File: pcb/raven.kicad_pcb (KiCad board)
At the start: 4 copper layers, 63.2 x 54.2 mm, 191 parts, among them J1 Conn_02x20_Odd_Even, J10 Conn_ARM_SWD_TagConnect_TC203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, J14 Conn_01x04_Pin, J15 Conn_01x04_Pin, J16 Conn_01x04_Pin, J17 Conn_01x04_Pin, J18 Conn_01x04_Pin, J2 Conn_01x04_MountingPin, J20 Screw_Terminal_01x02, J21 Conn_01x03_Pin, J22 Conn_01x03_Pin, J23 Conn_01x03_Pin, J24 Conn_01x03_Pin, J25 Conn_01x03_Pin, J26 Screw_Terminal_01x02, J27 Screw_Terminal_01x02, J28 Screw_Terminal_01x02, J29 Screw_Terminal_01x02, J3 Conn_01x02_Pin, J4 Conn_01x02_Pin, J5 Conn_01x04_MountingPin, J6 Conn_01x02_Pin, J7 Conn_01x02_Pin, J8 Conn_01x02_Pin, J9 Conn_01x02_Pin, SW1 SW_Push, SW2 SW_Push, U1 DRV8874PWPR, U2 ICM-42688-P, U3 QMC5883L, U30 DRV8874PWPR, U4 DRV8874PWPR, U5 DRV8874PWPR, U6 DRV8874PWPR, U7 STM32G431CBUx, U8 74HC595, U9 TPS548B28RWWR, Y1 16MHz

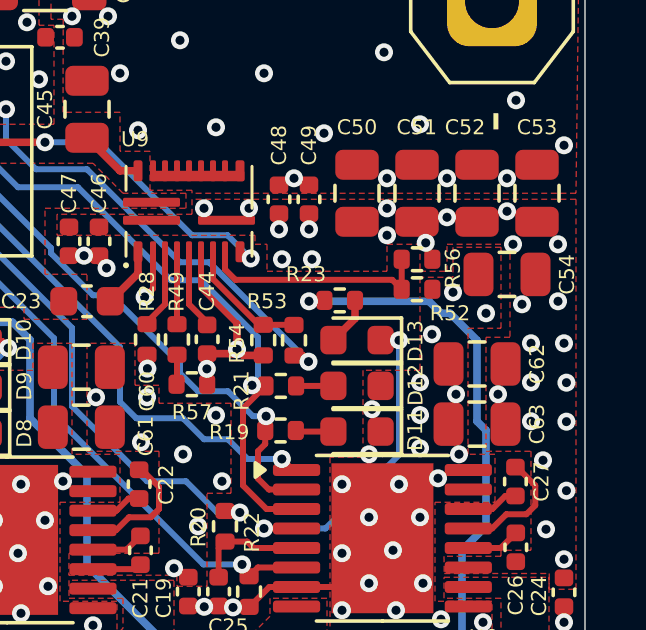
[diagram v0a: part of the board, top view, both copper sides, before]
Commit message: Change cutoff voltage
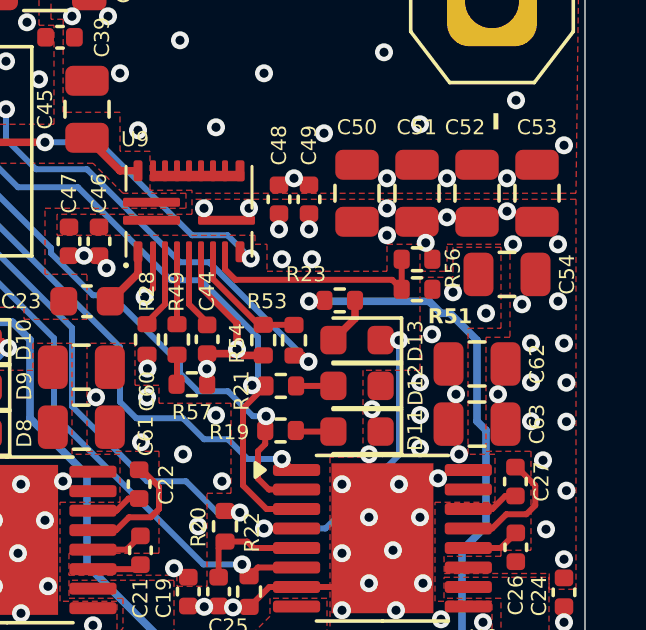
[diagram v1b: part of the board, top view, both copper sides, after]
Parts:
- removed R52: 12k, Resistor_SMD:R_0402_1005Metric
- added R51: 10k, Resistor_SMD:R_0402_1005Metric, F.Cu at (155.0, 80.0)

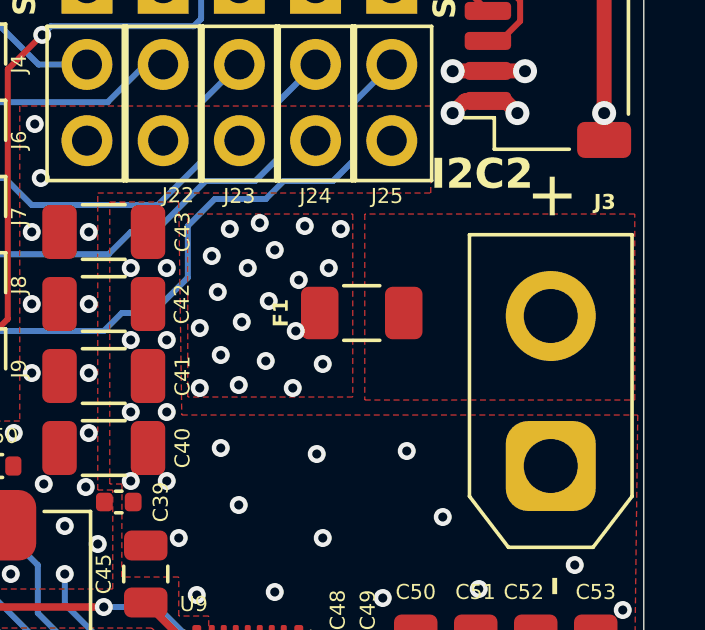
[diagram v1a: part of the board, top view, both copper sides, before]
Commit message: Plan adding power switch
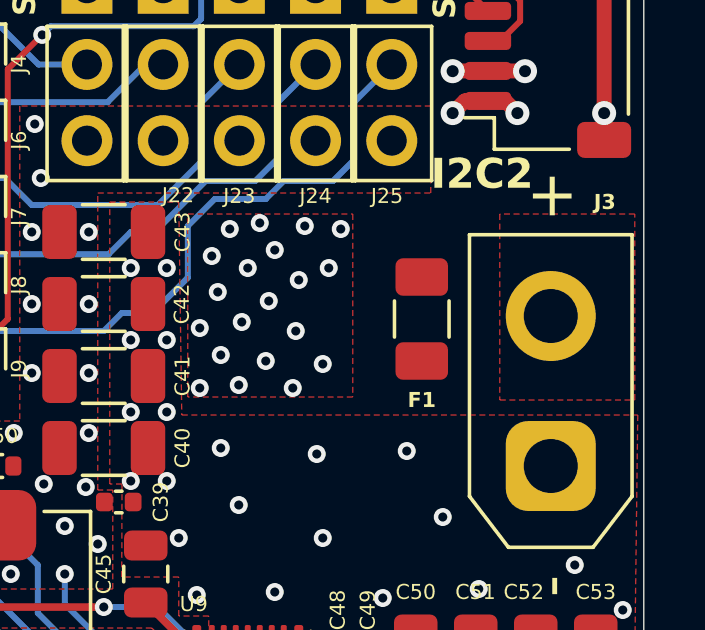
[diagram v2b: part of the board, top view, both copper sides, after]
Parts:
- moved F1 2.01 mm to (153.2, 65.5), turned to 90 degrees
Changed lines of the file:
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@@
 	(footprint "Fuse:Fuse_1206_3216Metric"
 		(layer "F.Cu")
-		(at 151.2 65.3)
+		(at 153.2 65.5 90)
 		(descr "Fuse SMD 1206 (3216 Metric), square (rectangular) end terminal, IPC_7351 nominal, (Body size source: http://www.tortai-tech.com/upload/download/2011102023233369053.pdf), generated with kicad-footprint-generator")
 		(tags "fuse")
 		(property "Reference" "F1"
-			(at -2.7 0 90)
+			(at -2.7 0 360)
 			(layer "F.SilkS")
 			(effects
@@
 		)
 		(property "Value" "Fuse"
-			(at 0 1.82 0)
+			(at 0 1.82 90)
 			(layer "F.Fab")
 			(effects
@@
 		)
 		(property "Footprint" "Fuse:Fuse_1206_3216Metric"
-			(at 0 0 0)
+			(at 0 0 90)
 			(unlocked yes)
 			(layer "F.Fab")
@@
 		)
 		(property "Datasheet" ""
-			(at 0 0 0)
+			(at 0 0 90)
 			(unlocked yes)
 			(layer "F.Fab")
@@
 		)
 		(property "Description" "Fuse"
-			(at 0 0 0)
+			(at 0 0 90)
 			(unlocked yes)
 			(layer "F.Fab")
@@
 		)
 		(property "LCSC" "C2838917"
-			(at 0 0 0)
+			(at 0 0 90)
 			(unlocked yes)
 			(layer "F.Fab")
@@
 		)
 		(fp_line
-			(start -2.28 -1.12)
-			(end 2.28 -1.12)
+			(start 2.28 -1.12)
+			(end 2.28 1.12)
 			(stroke
 				(width 0.05)
@@
 		)
 		(fp_line
-			(start -2.28 1.12)
-			(end -2.28 -1.12)
+			(start -2.28 -1.12)
+			(end 2.28 -1.12)
 			(stroke
 				(width 0.05)
@@
 		)
 		(fp_line
-			(start 2.28 -1.12)
-			(end 2.28 1.12)
+			(start 2.28 1.12)
+			(end -2.28 1.12)
 			(stroke
 				(width 0.05)
@@
 		)
 		(fp_line
-			(start 2.28 1.12)
-			(end -2.28 1.12)
+			(start -2.28 1.12)
+			(end -2.28 -1.12)
 			(stroke
 				(width 0.05)
@@
 		)
 		(fp_line
-			(start -1.6 -0.8)
-			(end 1.6 -0.8)
+			(start 1.6 -0.8)
+			(end 1.6 0.8)
 			(stroke
 				(width 0.1)
@@
 		)
 		(fp_line
-			(start -1.6 0.8)
-			(end -1.6 -0.8)
+			(start -1.6 -0.8)
+			(end 1.6 -0.8)
 			(stroke
 				(width 0.1)
@@
 		)
 		(fp_line
-			(start 1.6 -0.8)
-			(end 1.6 0.8)
+			(start 1.6 0.8)
+			(end -1.6 0.8)
 			(stroke
 				(width 0.1)
@@
 		)
 		(fp_line
-			(start 1.6 0.8)
-			(end -1.6 0.8)
+			(start -1.6 0.8)
+			(end -1.6 -0.8)
 			(stroke
 				(width 0.1)
@@
 		)
 		(fp_text user "${REFERENCE}"
-			(at 0 0 0)
+			(at 0 0 90)
 			(layer "F.Fab")
 			(effects
@@
 		)
 		(pad "1" smd roundrect
-			(at -1.399999 0)
+			(at -1.399999 0 90)
 			(size 1.25 1.75)
 			(layers "F.Cu" "F.Paste" "F.Mask")
@@
 		)
 		(pad "2" smd roundrect
-			(at 1.399999 0)
+			(at 1.399999 0 90)
 			(size 1.25 1.75)
 			(layers "F.Cu" "F.Paste" "F.Mask")
@@
 		(min_thickness 0.25)
 		(filled_areas_thickness no)
-		(fill yes
+		(fill
 			(thermal_gap 0.5)
 			(thermal_bridge_width 0.5)
@@
 		(polygon
 			(pts
-				(xy 151.3 68.2) (xy 160.3 68.2) (xy 160.3 62) (xy 151.3 62)
+				(xy 155.8 68.2) (xy 160.3 68.2) (xy 160.3 62) (xy 155.8 62)
 			)
 		)

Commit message: Add power switch
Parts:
- added J11: Conn_01x02_Pin, Connector_JST:JST_PH_B2B-PH-K_1x02_P2.00mm_Vertical, F.Cu at (149.8, 71.5)
- added Q1: DMP2002UPS, Footprints:DMP2002UPS, F.Cu at (148.8, 65.3)
- added R52: 10k, Resistor_SMD:R_0402_1005Metric, F.Cu at (150.1, 68.7)
- added R58: 10k, Resistor_SMD:R_0402_1005Metric, F.Cu at (152.1, 68.7)
- moved F1 1.60 mm to (153.1, 63.9), turned to -90 degrees
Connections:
- net /VDDF renamed Net-(J3-Pin_2)
- F1 pad 1: VDD -> Net-(F1-Pad1)
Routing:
- net Net-(J11-Pin_1): track 0.00 -> 4.67 mm
- net Net-(Q1-G): track 0.00 -> 3.26 mm
- net VDD: vias 91 -> 79
- net Net-(F1-Pad1): vias 0 -> 6
- net GND: vias 170 -> 167
- added copper zone on F.Cu, net Net-(F1-Pad1)

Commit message: Finish for revision 2 production
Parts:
- removed J25: Conn_01x03_Pin, Connector_PinHeader_2.54mm:PinHeader_1x03_P2.54mm_Vertical
- added C28: 10u, Capacitor_SMD:C_0603_1608Metric, F.Cu at (146.6, 67.6)
- added Q3: DMP2002UPS, Footprints:DMP2002UPS, F.Cu at (149.0, 63.9)
- added R66: 7k5, Resistor_SMD:R_0402_1005Metric, F.Cu at (153.4, 67.3)
- L1: value 330nH -> 1u; footprint Inductor_SMD:L_Changjiang_FXL0630 -> Footprints:L_0660A
- Q1: value DMP2002UPS -> AO3400A; footprint Footprints:DMP2002UPS -> Package_TO_SOT_SMD:SOT-23
- R24: value 10k -> 33k
- R25: value 1k5 -> 7k5
- R26, R28, R29, R30, R31, R32, R33, R34, R35, R36, R37, R38, R39, R40, R41, R42, R43, R44, R45, R46, R47, R48, R51, R52, R54, R55, R7, R8: value 10k -> 7k5
- R49: value 200k -> 7k5
- R53: value 75k -> 56k
- R56: value 100k -> 47k
- R57: value 47k -> 56k
- R58: value 10k -> 100k
- moved R49 14.5 mm to (149.0, 67.3), turned to 180 degrees
- moved R46 6.17 mm to (107.4, 77.3), turned to -90 degrees
- moved Q1 5.86 mm to (152.5, 69.8)
- moved R48 5.76 mm to (101.6, 75.1), turned to 90 degrees
- moved R43 4.78 mm to (107.4, 75.2)
- moved R39 4.39 mm to (102.6, 75.2)
- moved R58 3.12 mm to (149.0, 68.2), turned to 180 degrees
- moved R52 1.94 mm to (151.4, 67.3)
- moved R57 1.56 mm to (147.0, 81.7), turned to -90 degrees
- moved J11 1.55 mm to (148.4, 71.0), turned to -90 degrees
- moved D14 1.54 mm to (135.1, 69.8)
- moved C7 1.36 mm to (131.7, 54.4)
- moved C6 1.35 mm to (132.7, 54.4)
- moved C8 1.24 mm to (129.4, 56.5)
- moved U2 1.24 mm to (129.4, 54.5)
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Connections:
- D14 pad 1: /PGOOD -> GND
- D14 pad 2: Net-(D14-A) -> /PGOOD
- F1 pad 1: Net-(F1-Pad1) -> Net-(J3-Pin_2)
- F1 pad 2: Net-(J3-Pin_2) -> Net-(F1-Pad2)
- J14 pad 2: /MotorHub/Encoder1/BIN -> +5V
- J14 pad 4: +5V -> /MotorHub/Encoder1/BIN
- J15 pad 2: /MotorHub/Encoder2/BIN -> +5V
- J15 pad 4: +5V -> /MotorHub/Encoder2/BIN
- J16 pad 2: /MotorHub/Encoder3/BIN -> +5V
- J16 pad 4: +5V -> /MotorHub/Encoder3/BIN
- J17 pad 2: /MotorHub/Encoder4/BIN -> +5V
- J17 pad 4: +5V -> /MotorHub/Encoder4/BIN
- J18 pad 2: /MotorHub/Encoder5/BIN -> +5V
- J18 pad 4: +5V -> /MotorHub/Encoder5/BIN
- J21 pad 2: /MotorHub/SIG1 -> +5V
- J21 pad 3: +5V -> /MotorHub/SIG1
- J22 pad 2: /MotorHub/SIG2 -> +5V
- J22 pad 3: +5V -> /MotorHub/SIG2
- J23 pad 2: /MotorHub/SIG3 -> +5V
- J23 pad 3: +5V -> /MotorHub/SIG3
- J24 pad 2: /MotorHub/SIG4 -> +5V
- J24 pad 3: +5V -> /MotorHub/SIG4
- Q1 pad 1: VDD -> /PWR
- Q1 pad 2: VDD -> GND
- Q1 pad 3: VDD -> Net-(Q1-D)
- R49 pad 1: Net-(R49-Pad1) -> /PWR
- R49 pad 2: /MD -> GND
- R50 pad 1: Net-(D14-A) -> /PGOOD
- R52 pad 1: Net-(Q1-G) -> Net-(Q3-G)
- R52 pad 2: VDD -> Net-(Q1-D)
- R57 pad 1: Net-(R49-Pad1) -> /MD
- R58 pad 1: Net-(Q1-G) -> Net-(J11-Pin_1)
- R58 pad 2: Net-(J11-Pin_1) -> Net-(Q1-D)
- U7 pad 3: /MotorHub/B5 -> /MotorHub/A5
- U7 pad 30: /MotorHub/SIG5 -> /PWR
- U7 pad 33: /MotorHub/SIG2 -> /MotorHub/SIG1
- U7 pad 34: /MotorHub/SIG1 -> /MotorHub/SIG2
- U7 pad 4: /MotorHub/A5 -> /MotorHub/B5
- U7 pad 43: /MotorHub/B1 -> /MotorHub/A1
- U7 pad 44: /MotorHub/A1 -> /MotorHub/B1
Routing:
- net /MotorHub/SIG5: track 39.1 -> 0.00 mm, vias 1 -> 0
- net /PWR: track 0.00 -> 36.4 mm, vias 0 -> 2
- net /MotorHub/Encoder4/BIN: track 12.7 -> 3.27 mm
- net Net-(Q1-D): track 0.00 -> 8.03 mm, vias 0 -> 2
- net /MotorHub/Encoder2/BIN: track 11.2 -> 3.27 mm
- net Net-(Q3-G): track 0.00 -> 7.73 mm, vias 0 -> 2
- net /MotorHub/Encoder1/BIN: track 9.86 -> 3.26 mm
- net /MotorHub/Encoder3/BIN: track 9.18 -> 3.27 mm
- net GND: track 123.5 -> 128.1 mm, vias 167 -> 170
- net /MotorHub/B5: track 25.0 -> 20.8 mm
- net /PGOOD: track 20.3 -> 24.1 mm
- net +3V3: track 274.9 -> 271.0 mm
- net /MotorHub/Encoder2/AIN: track 10.2 -> 6.45 mm
- net /MotorHub/A5: track 21.7 -> 25.2 mm
- net Net-(Q1-G): track 3.26 -> 0.00 mm
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- added copper zone on F.Cu, net Net-(F1-Pad2)
- removed copper zone on F.Cu, net Net-(F1-Pad1)

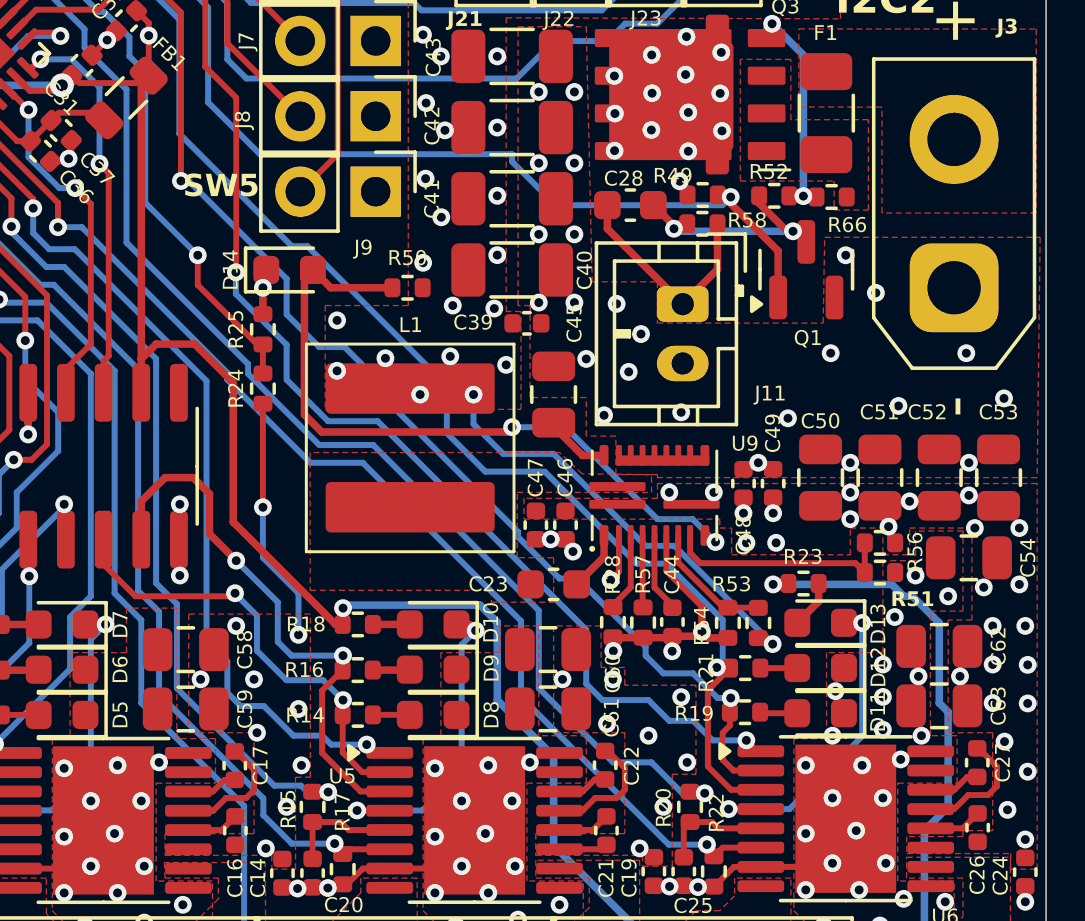
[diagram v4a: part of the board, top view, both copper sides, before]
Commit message: Add vsense kelvin connections
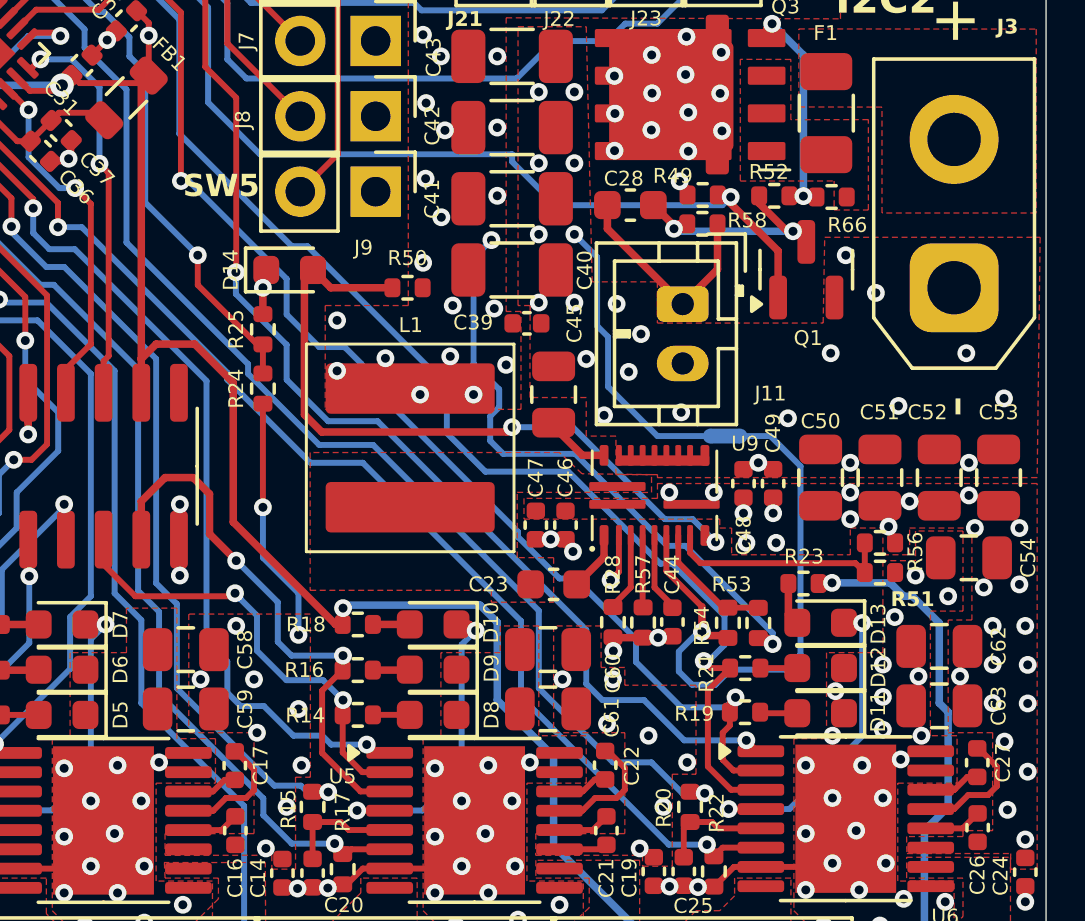
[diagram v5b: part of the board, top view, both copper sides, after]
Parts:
- added NT1: NetTie_2, NetTie:NetTie-2_SMD_Pad0.5mm, B.Cu at (149.8, 75.4)
- turned R23 to 180 degrees
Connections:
- R54 pad 2: GND -> Net-(U9-VSNS)
- U9 pad 6: GND -> Net-(U9-VSNS)
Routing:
- net Net-(U9-VSNS): track 0.00 -> 20.1 mm, vias 0 -> 1
- net +5V: track 17.9 -> 23.8 mm
- net GND: track 128.1 -> 132.0 mm, vias 170 -> 169
- net +3V3: track 271.0 -> 269.0 mm
- net /MotorHub/PH5: track 42.8 -> 43.6 mm
- net /MotorHub/SL5: track 51.6 -> 52.4 mm
- net VDD: vias 84 -> 83
